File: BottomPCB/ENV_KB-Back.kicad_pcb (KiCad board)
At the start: 2 copper layers, 354.6 x 156.1 mm, 8 parts

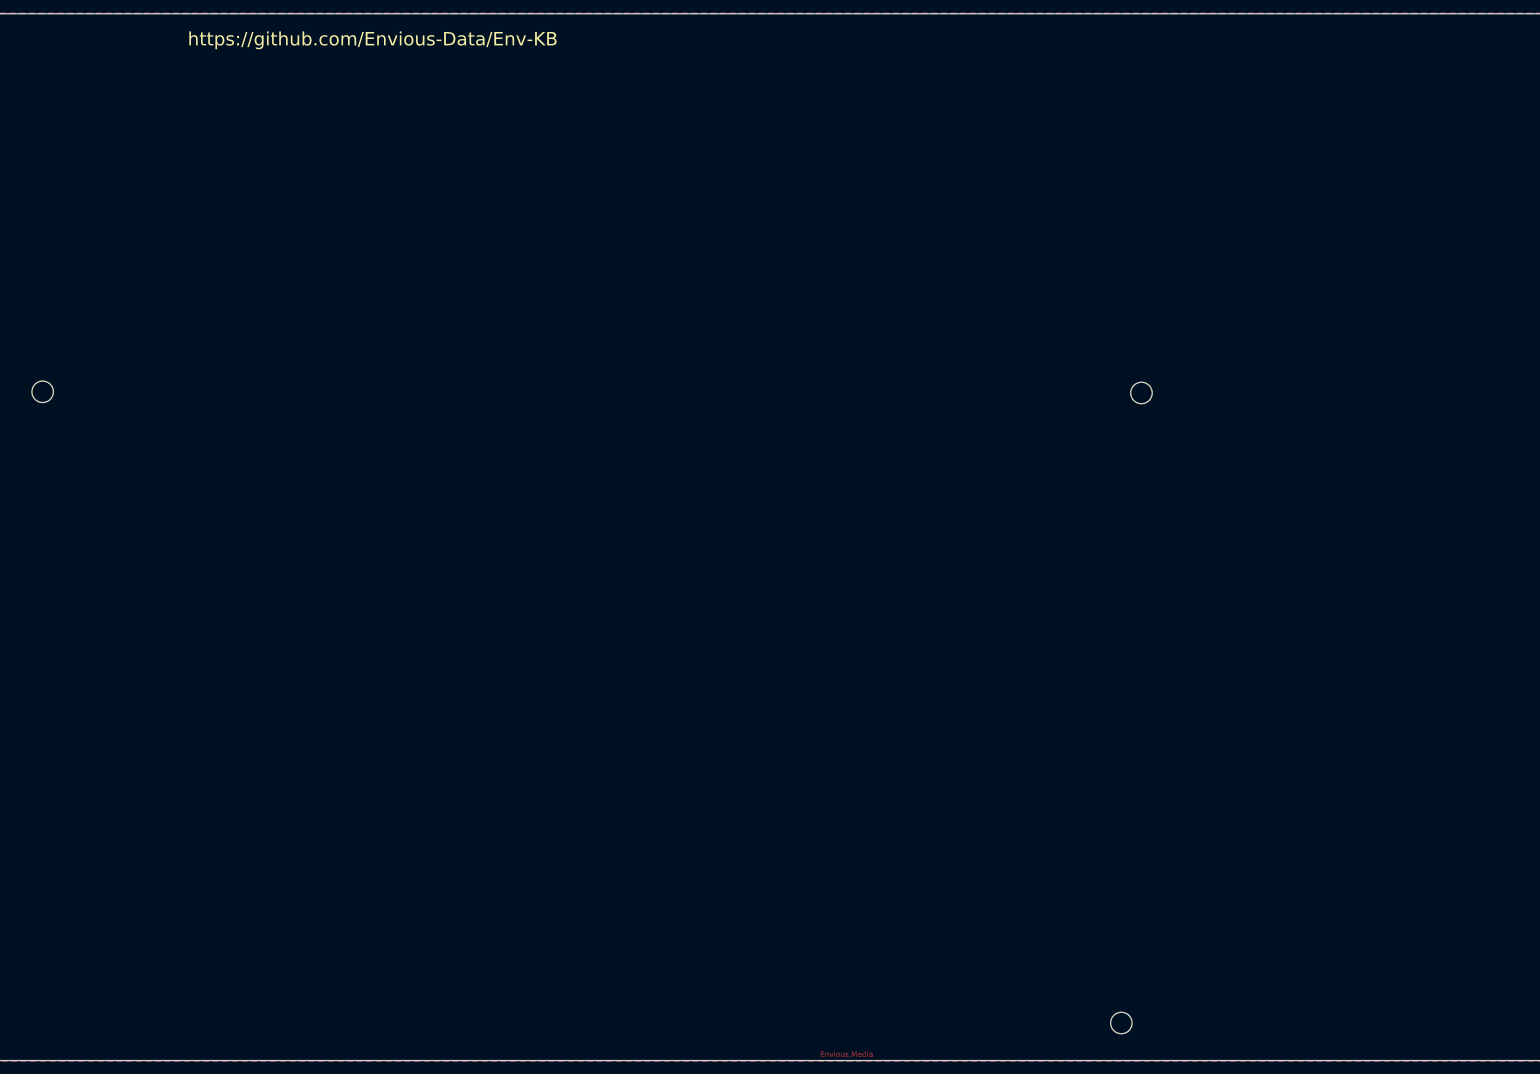
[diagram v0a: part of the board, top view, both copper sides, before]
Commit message: changed type-c port and re-did some bits
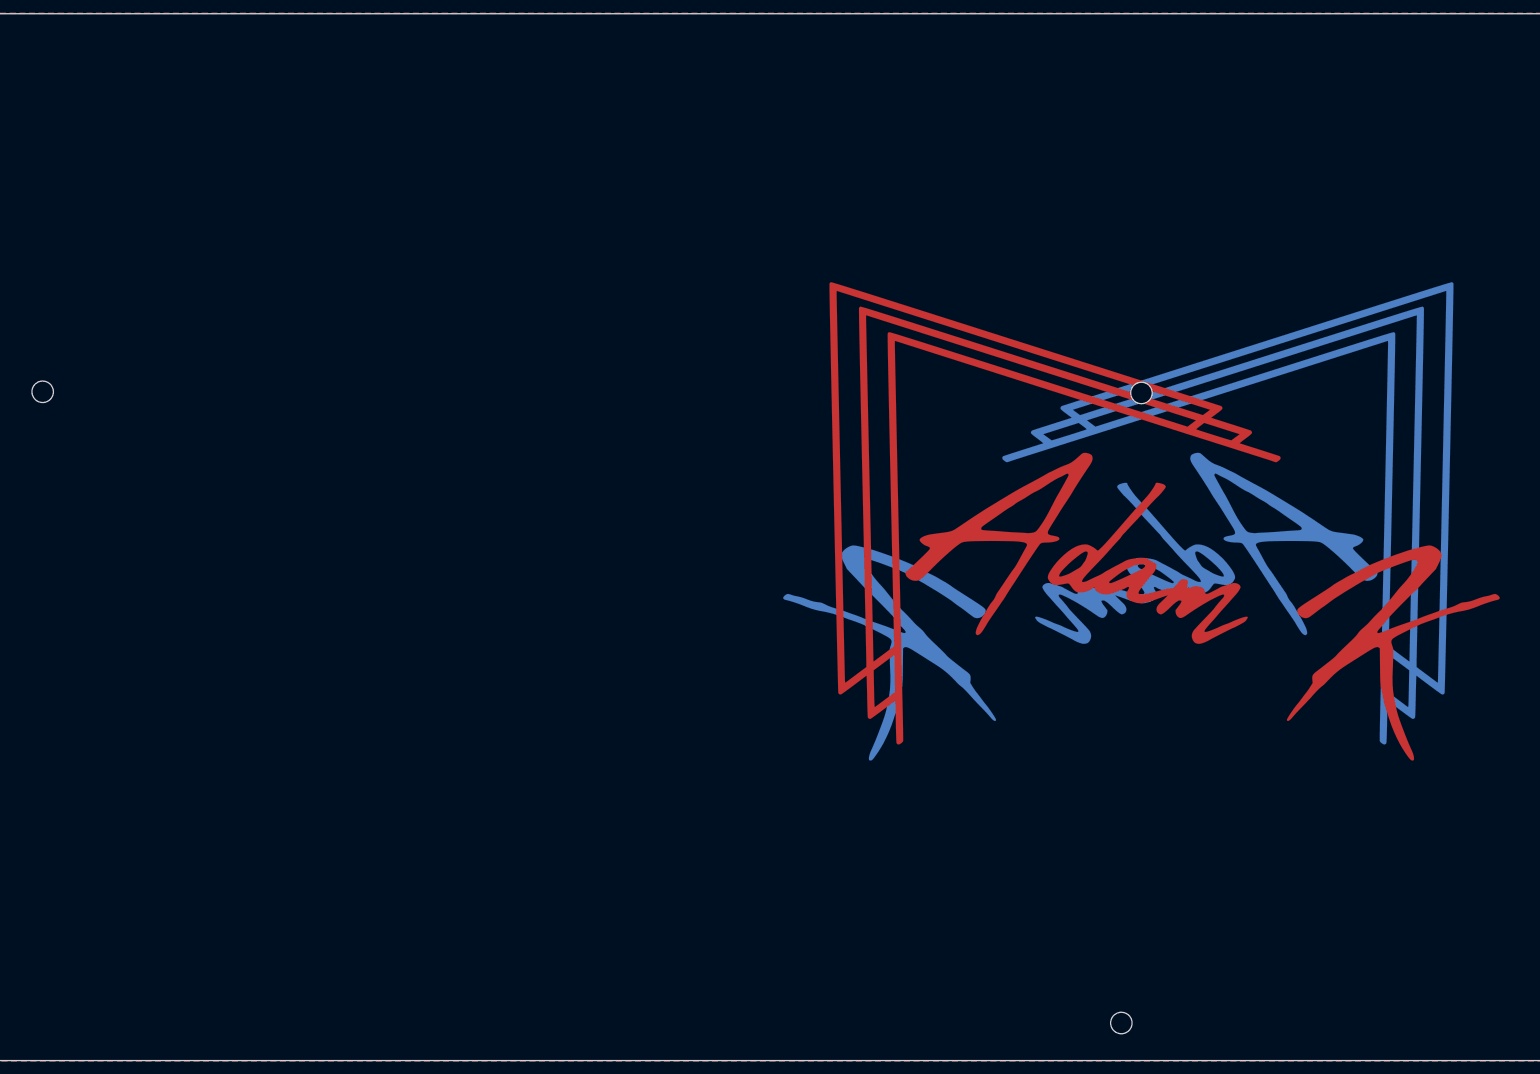
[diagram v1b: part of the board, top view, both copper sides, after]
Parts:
- added G***: LOGO, EM_Logo:LargeLogo, B.Cu at (212.2, 137.7)
- added G***: LOGO, EM_Logo:LargeLogo, F.Cu at (212.2, 137.7)
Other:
- board text removed: "Envious.Media"
- board text removed: "https://github.com/Envious-Data/Env-KB"

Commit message: Changed Logo and fixed missing silkscreen for I2C header
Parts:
- removed the G*** at (212.2, 137.7) (x2)
- added G***: LOGO, EM_Logo:newlogoinverted, B.Cu at (212.2, 137.7)
- added G***: LOGO, EM_Logo:newlogoinverted, F.Cu at (212.2, 137.7)
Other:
- board text added: "http://github.com/Envious-Data/Env-KB"
- board text removed: "PLEASE CHECK ALIGNMENT OF "TYPE-C-31-M-12" or "J0""

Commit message: Corrected some netlist issues on backplate and switch plate + cleanup of stuff.
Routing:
- added copper zone on B.Cu, net (none)
- added copper zone on F.Cu, net (none)
- removed copper zone on B.Cu, net GND
- removed copper zone on F.Cu, net GND

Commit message: Changed all mount holes to M2 and added some pads around the holes to avoid scratches being visible on pcbs
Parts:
- H0, H1, H10, H3, H4, H6, H7, H9: footprint MountingHole:MountingHole_3.2mm_M3 -> MountingHole:MountingHole_2.2mm_M2_Pad
- moved G*** 3.00 mm to (212.2, 134.7) (x2)

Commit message: updated backPCB with new mount hole
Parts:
- removed G*** (x2): LOGO, EM_Logo:newlogoinverted
- added H11: MountingHole, MountingHole:MountingHole_2.2mm_M2_Pad, F.Cu at (192.3, 63.4)
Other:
- net class DIFF removed
- net class Default removed
